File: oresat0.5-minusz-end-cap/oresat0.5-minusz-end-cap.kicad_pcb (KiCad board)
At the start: 2 copper layers, 105.6 x 105.6 mm, 46 parts, among them J2 U.FL-R-SMA, U1 LTC4305IGN, U2 MMC5983MA, U3 MMC5983MA

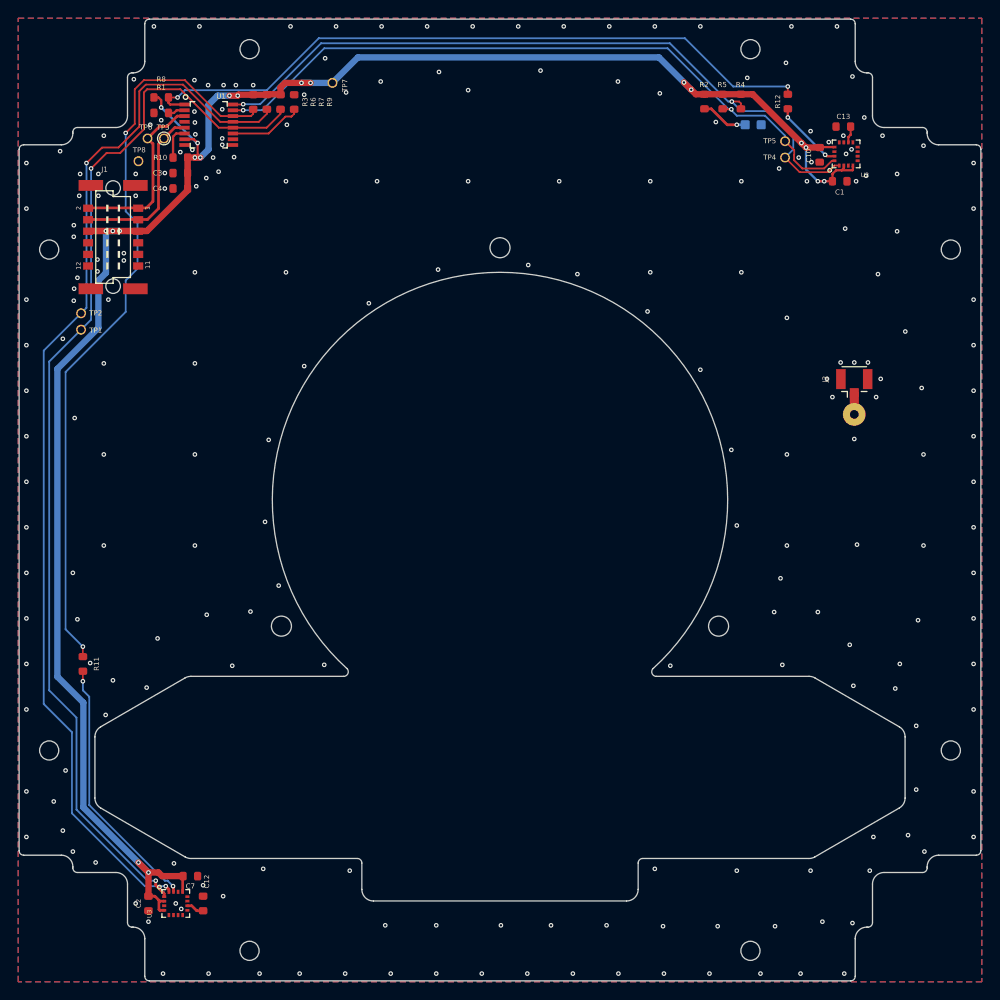
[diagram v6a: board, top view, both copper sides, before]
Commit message: OreSat 0.5 Endcaps (+Z v1.3 and -Z v1.2) ready for ordering, reviewed -Z endcap, made small library and neatness changes to +Z endcap
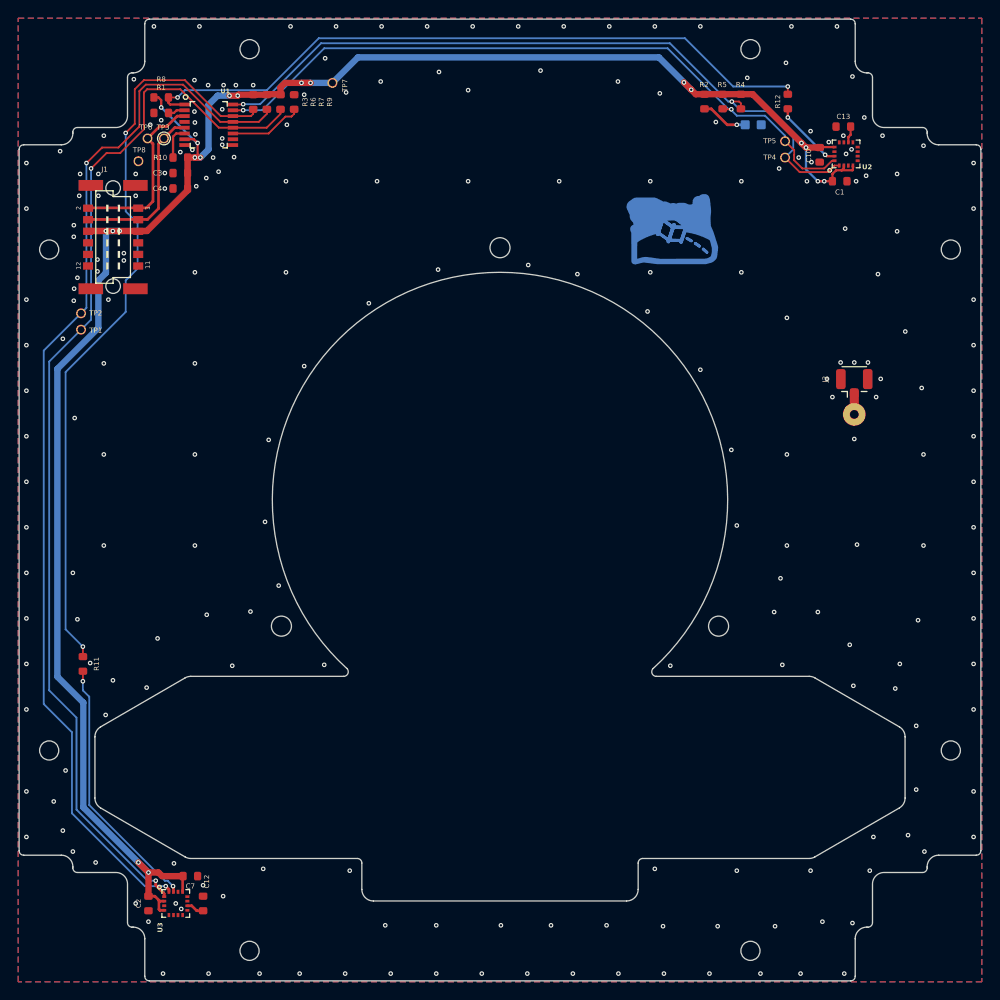
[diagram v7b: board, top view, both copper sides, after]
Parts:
- added LOGO1: , oresat-graphics:PSAS_LOGO_10X10, B.Cu at (130.0, 75.5)
- added REF**: logo-small, oresat-graphics:logo-small, B.Cu at (167.5, 75.0)
- C1, C10, C2, C3, C7: value ~ -> 100n
- C12, C13, C4: value ~ -> 10u
- R1, R10, R3, R4, R5, R6, R7, R8, R9: value ~ -> 4.7k
- R2: value ~ -> 2.7k
- U1: value LTC4305IGN -> LTC4305; footprint oresat0.5-minusz-end-cap:16-SSOP -> oresat-ics:16-SSOP
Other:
- board text added: "2024/03/20"
- board text removed: "2024/03/04"

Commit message: Fixed issues 5 and 6 -- weird 4.7k values everywhere, missing libraries, and used no-place to indicate actual no place components.
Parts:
- D2: value ~ -> GRN
- J1: value ~ -> M55-7011242R
- R11, R12: value NP -> 2.7k
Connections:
- net 3.3V renamed +3.3V
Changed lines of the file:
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@@
 	)
 	(net 0 "")
-	(net 1 "3.3V")
+	(net 1 "+3.3V")
 	(net 2 "Net-(ANT1-A)")
 	(net 3 "Net-(U3-CAP)")
@@
 			(size 0.3 0.45)
 			(layers "F.Cu" "F.Paste" "F.Mask")
-			(net 1 "3.3V")
+			(net 1 "+3.3V")
 			(pinfunction "VDD")
 			(pintype "power_in")
@@
 			(size 0.3 0.45)
 			(layers "F.Cu" "F.Paste" "F.Mask")
-			(net 1 "3.3V")
+			(net 1 "+3.3V")
 			(pinfunction "SPI_CS")
 			(pintype "input")
@@
 			(size 0.3 0.45)
 			(layers "F.Cu" "F.Paste" "F.Mask")
-			(net 1 "3.3V")
+			(net 1 "+3.3V")
 			(pinfunction "VDDIO")
 			(pintype "power_in")
@@
 			(layers "F.Cu" "F.Paste" "F.Mask")
 			(roundrect_rratio 0.25)
-			(net 1 "3.3V")
+			(net 1 "+3.3V")
 			(pinfunction "1")
 			(pintype "passive")
@@
 			(size 1.143 0.4191)
 			(layers "F.Cu" "F.Paste" "F.Mask")
-			(net 1 "3.3V")
+			(net 1 "+3.3V")
 			(pinfunction "VCC")
 			(pintype "power_in")
@@
 			)
 		)
-		(property "Value" "NP"
+		(property "Value" "2.7k"
 			(at -1.2 1.6 90)
 			(layer "F.Fab")
@@
 		(sheetname "Root")
 		(sheetfile "oresat0.5-minusz-end-cap.kicad_sch")
+		(attr dnp)
 		(fp_line
 			(start 1.495 -0.745)
@@
 			(layers "F.Cu" "F.Paste" "F.Mask")
 			(roundrect_rratio 0.25)
-			(net 1 "3.3V")
+			(net 1 "+3.3V")
 			(pinfunction "1")
 			(pintype "passive")
@@
 			(layers "F.Cu" "F.Paste" "F.Mask")
 			(roundrect_rratio 0.25)
-			(net 1 "3.3V")
+			(net 1 "+3.3V")
 			(pinfunction "2")
 			(pintype "passive")
@@
 			(size 0.3 0.45)
 			(layers "F.Cu" "F.Paste" "F.Mask")
-			(net 1 "3.3V")
+			(net 1 "+3.3V")
 			(pinfunction "VDD")
 			(pintype "power_in")
@@
 			(size 0.3 0.45)
 			(layers "F.Cu" "F.Paste" "F.Mask")
-			(net 1 "3.3V")
+			(net 1 "+3.3V")
 			(pinfunction "SPI_CS")
 			(pintype "input")
@@
 			(size 0.3 0.45)
 			(layers "F.Cu" "F.Paste" "F.Mask")
-			(net 1 "3.3V")
+			(net 1 "+3.3V")
 			(pinfunction "VDDIO")
 			(pintype "power_in")
@@
 			)
 		)
-		(property "Value" "NP"
+		(property "Value" "2.7k"
 			(at -1.2 1.6 90)
 			(layer "F.Fab")
@@
 		(sheetname "Root")
 		(sheetfile "oresat0.5-minusz-end-cap.kicad_sch")
+		(attr dnp)
 		(fp_line
 			(start 1.495 -0.745)
@@
 			(layers "F.Cu" "F.Paste" "F.Mask")
 			(roundrect_rratio 0.25)
-			(net 1 "3.3V")
+			(net 1 "+3.3V")
 			(pinfunction "1")
 			(pintype "passive")
@@
 			(layers "F.Cu" "F.Paste" "F.Mask")
 			(roundrect_rratio 0.25)
-			(net 1 "3.3V")
+			(net 1 "+3.3V")
 			(pinfunction "1")
 			(pintype "passive")
@@
 			(layers "F.Cu" "F.Paste" "F.Mask")
 			(roundrect_rratio 0.25)
-			(net 1 "3.3V")
+			(net 1 "+3.3V")
 			(pinfunction "2")
 			(pintype "passive")
@@
 			(layers "F.Cu" "F.Paste" "F.Mask")
 			(roundrect_rratio 0.25)
-			(net 1 "3.3V")
+			(net 1 "+3.3V")
 			(pinfunction "2")
 			(pintype "passive")
@@
 			(layers "F.Cu" "F.Paste" "F.Mask")
 			(roundrect_rratio 0.25)
-			(net 1 "3.3V")
+			(net 1 "+3.3V")
 			(pinfunction "1")
 			(pintype "passive")
@@
 			(layers "F.Cu" "F.Paste" "F.Mask")
 			(roundrect_rratio 0.25)
-			(net 1 "3.3V")
+			(net 1 "+3.3V")
 			(pinfunction "2")
 			(pintype "passive")
@@
 			(layers "F.Cu" "F.Paste" "F.Mask")
 			(roundrect_rratio 0.25)
-			(net 1 "3.3V")
+			(net 1 "+3.3V")
 			(pinfunction "2")
 			(pintype "passive")
@@
 			)
 		)
-		(property "Value" "~"
+		(property "Value" "M55-7011242R"
 			(at 0 0 90)
 			(layer "F.Fab")
@@
 			(size 0.8 1.1)
 			(layers "F.Cu" "F.Paste" "F.Mask")
-			(net 1 "3.3V")
+			(net 1 "+3.3V")
 			(pinfunction "5")
 			(pintype "passive")
@@
 			(size 0.8 1.1)
 			(layers "F.Cu" "F.Paste" "F.Mask")
-			(net 1 "3.3V")
+			(net 1 "+3.3V")
 			(pinfunction "6")
 			(pintype "passive")
@@
 			(layers "F.Cu" "F.Paste" "F.Mask")
 			(roundrect_rratio 0.25)
-			(net 1 "3.3V")
+			(net 1 "+3.3V")
 			(pinfunction "2")
 			(pintype "passive")
@@
 			(layers "F.Cu" "F.Paste" "F.Mask")
 			(roundrect_rratio 0.25)
-			(net 1 "3.3V")
+			(net 1 "+3.3V")
 			(pinfunction "2")
 			(pintype "passive")
@@
 			(layers "F.Cu" "F.Paste" "F.Mask")
 			(roundrect_rratio 0.25)
-			(net 1 "3.3V")
+			(net 1 "+3.3V")
 			(pinfunction "1")
 			(pintype "passive")
@@
 			(layers "F.Cu" "F.Paste" "F.Mask")
 			(roundrect_rratio 0.25)
-			(net 1 "3.3V")
+			(net 1 "+3.3V")
 			(pinfunction "2")
 			(pintype "passive")
@@
 			(layers "*.Cu" "*.Mask")
 			(remove_unused_layers no)
-			(net 1 "3.3V")
+			(net 1 "+3.3V")
 			(pinfunction "1")
 			(pintype "passive")
@@
 			)
 		)
-		(property "Value" "~"
+		(property "Value" "GRN"
 			(at 0 -0.635 0)
 			(layer "B.Fab")
